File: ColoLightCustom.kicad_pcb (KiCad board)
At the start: 2 copper layers, 41.1 x 65.5 mm, 4 parts, among them J1 Conn_01x05_Male, J2 Conn_01x05_Male

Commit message: Version 0.1
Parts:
- added J3: Conn_01x03, halibs:SolderPads3, F.Cu at (142.2, 108.6)
- added J4: Conn_01x03_Male, Connector_PinHeader_2.54mm:PinHeader_1x03_P2.54mm_Vertical, F.Cu at (151.5, 73.4)
- added REF**: WEEE-Logo_4.2x6mm_SilkScreen, Symbol:WEEE-Logo_4.2x6mm_SilkScreen, B.Cu at (142.2, 103.5)
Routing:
- net Net-(J1-Pad3): track 0.00 -> 34.1 mm
- net +5V: track 16.1 -> 41.3 mm
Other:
- net class 5V added: clearance 0.3, trace_width 0.5, via_dia 0.8, via_drill 0.4
- board text added: "5V"
- board text added: "DIN"
- board text added: "GND"
- board text added: "haus-automatisierung.com v0.1"

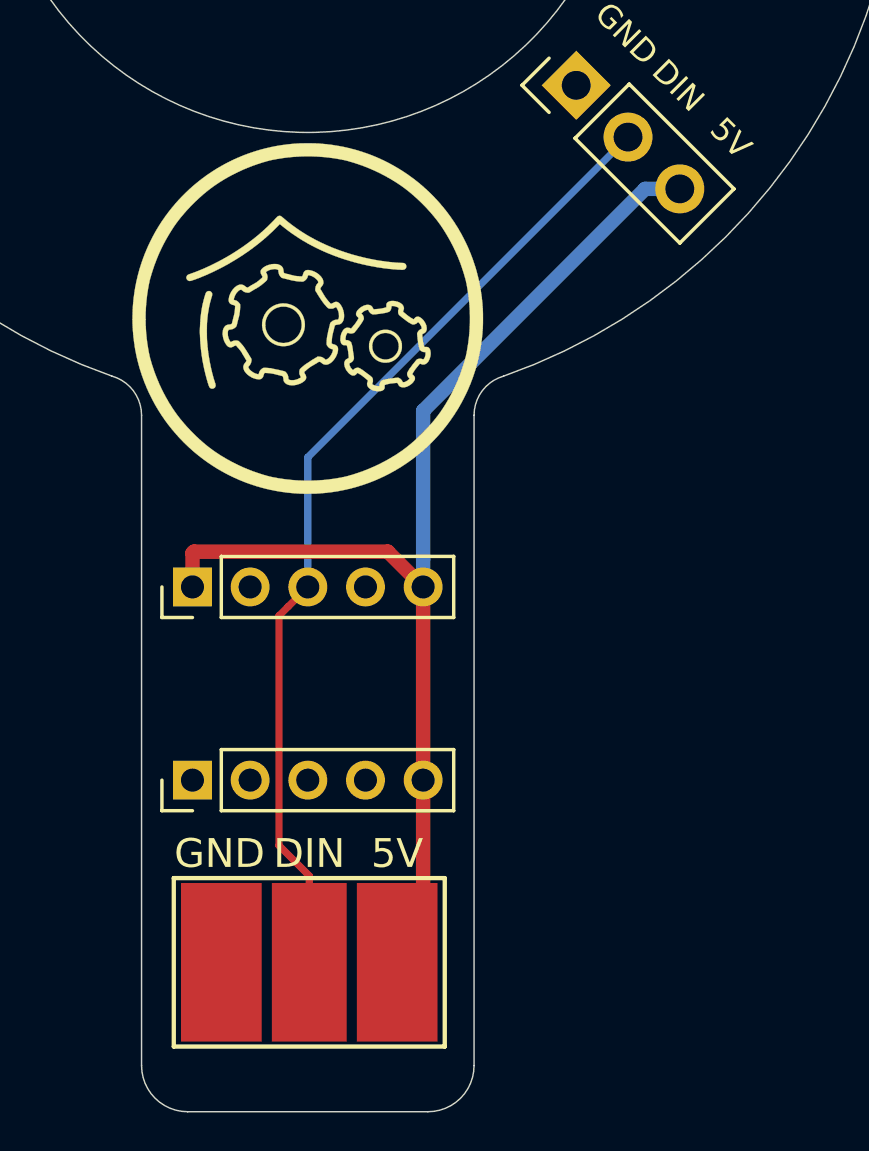
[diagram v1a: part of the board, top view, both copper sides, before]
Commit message: Changed thickness of lanes
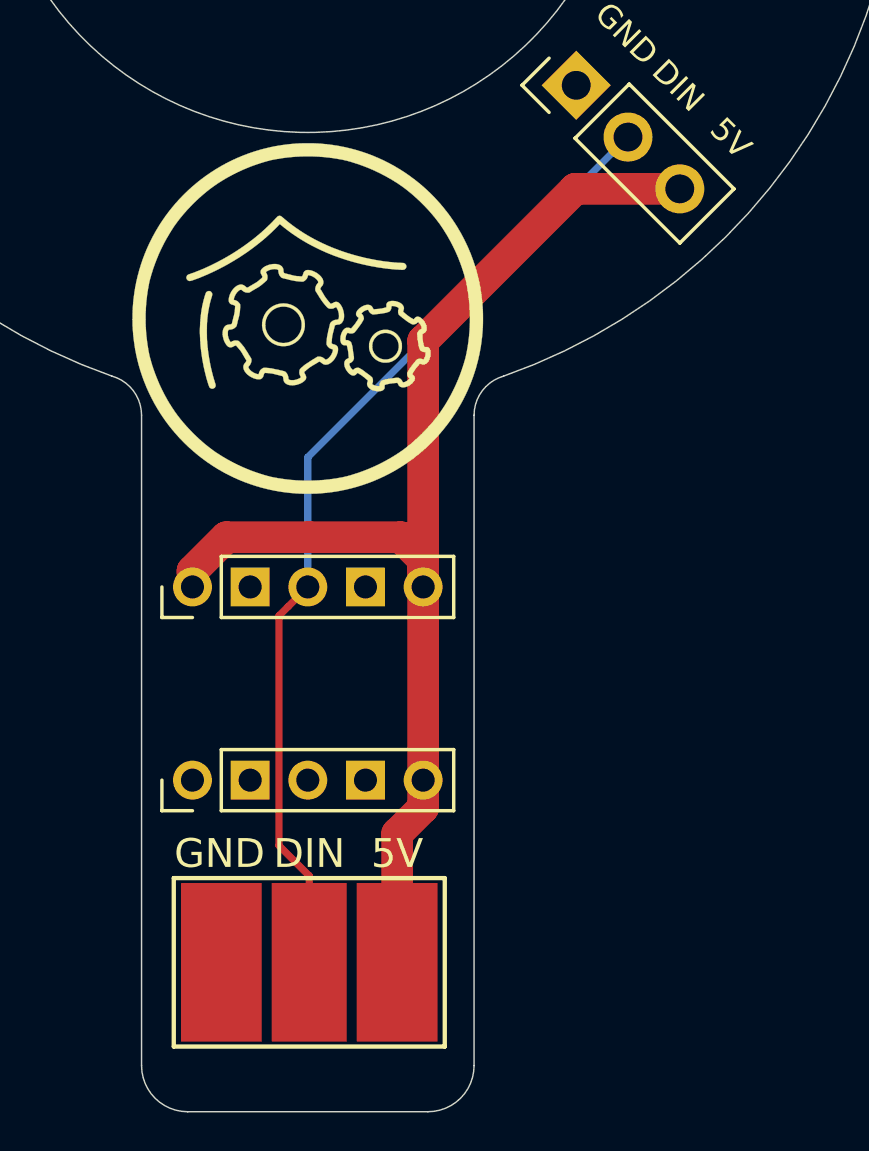
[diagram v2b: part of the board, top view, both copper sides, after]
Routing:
- net +5V: track 41.3 -> 43.3 mm
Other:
- net class 5V: clearance 0.3 -> 0.2; trace_width 0.5 -> 1.1
- board text added: "haus-automatisierung.com v0.2"
- board text removed: "haus-automatisierung.com v0.1"
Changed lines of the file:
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@@
     (thickness 1.6)
     (drawings 27)
-    (tracks 18)
+    (tracks 20)
     (zones 0)
     (modules 7)
@@
   (title_block
     (title "ColoLight Custom Controller")
-    (date 2019-11-17)
-    (rev 0.1)
+    (date 2019-11-19)
+    (rev 0.2)
     (company haus-automatisierung.com)
     (comment 1 "Matthias Kleine")
@@
     (mod_text_size 1 1)
     (mod_text_width 0.15)
-    (pad_size 2.6 5.5)
-    (pad_drill 0)
+    (pad_size 1.35 1.35)
+    (pad_drill 0.8)
     (pad_to_mask_clearance 0.051)
     (solder_mask_min_width 0.25)
@@
   )
   (net_class 5V ""
-    (clearance 0.3)
-    (trace_width 0.5)
+    (clearance 0.2)
+    (trace_width 1.1)
     (via_dia 0.8)
     (via_drill 0.4)
@@
     (pad 5 thru_hole oval (at 0 8 90) (size 1.35 1.35) (drill 0.8) (layers *.Cu *.Mask)
       (net 4 +5V))
-    (pad 4 thru_hole oval (at 0 6 90) (size 1.35 1.35) (drill 0.8) (layers *.Cu *.Mask)
+    (pad 4 thru_hole rect (at 0 6 90) (size 1.35 1.35) (drill 0.8) (layers *.Cu *.Mask)
       (net 5 GND))
     (pad 3 thru_hole oval (at 0 4 90) (size 1.35 1.35) (drill 0.8) (layers *.Cu *.Mask)
       (net 1 "Net-(J1-Pad3)"))
-    (pad 2 thru_hole oval (at 0 2 90) (size 1.35 1.35) (drill 0.8) (layers *.Cu *.Mask)
+    (pad 2 thru_hole rect (at 0 2 90) (size 1.35 1.35) (drill 0.8) (layers *.Cu *.Mask)
       (net 5 GND))
-    (pad 1 thru_hole rect (at 0 0 90) (size 1.35 1.35) (drill 0.8) (layers *.Cu *.Mask)
+    (pad 1 thru_hole circle (at 0 0 90) (size 1.35 1.35) (drill 0.8) (layers *.Cu *.Mask)
       (net 4 +5V))
     (model ${KISYS3DMOD}/Connector_PinHeader_2.00mm.3dshapes/PinHeader_1x05_P2.00mm_Vertical.wrl
@@
       (effects (font (size 1 1) (thickness 0.15)))
     )
-    (pad 1 thru_hole rect (at 0 0 90) (size 1.35 1.35) (drill 0.8) (layers *.Cu *.Mask)
+    (pad 1 thru_hole circle (at 0 0 90) (size 1.35 1.35) (drill 0.8) (layers *.Cu *.Mask)
       (net 2 "Net-(J2-Pad1)"))
-    (pad 2 thru_hole oval (at 0 2 90) (size 1.35 1.35) (drill 0.8) (layers *.Cu *.Mask)
+    (pad 2 thru_hole rect (at 0 2 90) (size 1.35 1.35) (drill 0.8) (layers *.Cu *.Mask)
       (net 5 GND))
     (pad 3 thru_hole oval (at 0 4 90) (size 1.35 1.35) (drill 0.8) (layers *.Cu *.Mask)
       (net 3 "Net-(J2-Pad3)"))
-    (pad 4 thru_hole oval (at 0 6 90) (size 1.35 1.35) (drill 0.8) (layers *.Cu *.Mask)
+    (pad 4 thru_hole rect (at 0 6 90) (size 1.35 1.35) (drill 0.8) (layers *.Cu *.Mask)
       (net 5 GND))
     (pad 5 thru_hole oval (at 0 8 90) (size 1.35 1.35) (drill 0.8) (layers *.Cu *.Mask)
@@
     )
   )
-  (gr_text "haus-automatisierung.com\nv0.1" (at 142.1638 49.5301) (layer B.SilkS)
+  (gr_text "haus-automatisierung.com\nv0.2" (at 142.1638 49.5301) (layer B.SilkS)
     (effects (font (size 1 1) (thickness 0.15)) (justify mirror))
   )
@@
   (segment (start 142.1638 86.345302) (end 142.1638 90.8422) (width 0.25) (layer B.Cu) (net 1))
   (segment (start 153.268951 75.240151) (end 142.1638 86.345302) (width 0.25) (layer B.Cu) (net 1))
-  (segment (start 146.1638 102.9594) (end 145.2626 103.8606) (width 0.5) (layer F.Cu) (net 4))
-  (segment (start 146.1638 97.5422) (end 146.1638 102.9594) (width 0.5) (layer F.Cu) (net 4))
-  (segment (start 146.1638 97.5422) (end 146.1638 90.8422) (width 0.5) (layer F.Cu) (net 4))
-  (segment (start 146.1638 89.887606) (end 146.1638 90.8422) (width 0.5) (layer B.Cu) (net 4))
-  (segment (start 146.1638 84.735323) (end 146.1638 89.887606) (width 0.5) (layer B.Cu) (net 4))
-  (segment (start 153.862921 77.036202) (end 146.1638 84.735323) (width 0.5) (layer B.Cu) (net 4))
-  (segment (start 155.065002 77.036202) (end 153.862921 77.036202) (width 0.5) (layer B.Cu) (net 4))
-  (segment (start 138.1638 89.6672) (end 138.1638 90.8422) (width 0.5) (layer F.Cu) (net 4))
-  (segment (start 144.938799 89.617199) (end 138.213801 89.617199) (width 0.5) (layer F.Cu) (net 4))
-  (segment (start 138.213801 89.617199) (end 138.1638 89.6672) (width 0.5) (layer F.Cu) (net 4))
-  (segment (start 146.1638 90.8422) (end 144.938799 89.617199) (width 0.5) (layer F.Cu) (net 4))
+  (segment (start 146.1638 98.496794) (end 145.2626 99.397994) (width 1.1) (layer F.Cu) (net 4))
+  (segment (start 145.2626 99.397994) (end 145.2626 103.8606) (width 1.1) (layer F.Cu) (net 4))
+  (segment (start 146.1638 97.5422) (end 146.1638 98.496794) (width 1.1) (layer F.Cu) (net 4))
+  (segment (start 146.1638 97.5422) (end 146.1638 90.8422) (width 1.1) (layer F.Cu) (net 4))
+  (segment (start 139.335799 89.117199) (end 138.1638 90.289198) (width 1.1) (layer F.Cu) (net 4))
+  (segment (start 146.1638 89.887606) (end 145.393393 89.117199) (width 1.1) (layer F.Cu) (net 4))
+  (segment (start 138.1638 90.289198) (end 138.1638 90.8422) (width 1.1) (layer F.Cu) (net 4))
+  (segment (start 146.1638 90.8422) (end 146.1638 89.887606) (width 1.1) (layer F.Cu) (net 4))
+  (segment (start 142.213301 89.117199) (end 139.335799 89.117199) (width 1.1) (layer F.Cu) (net 4))
+  (segment (start 145.393393 89.117199) (end 142.213301 89.117199) (width 1.1) (layer F.Cu) (net 4))
+  (segment (start 155.065002 77.036202) (end 151.436798 77.036202) (width 1.1) (layer F.Cu) (net 4))
+  (segment (start 146.1638 82.3092) (end 146.1638 90.8422) (width 1.1) (layer F.Cu) (net 4))
+  (segment (start 151.436798 77.036202) (end 146.1638 82.3092) (width 1.1) (layer F.Cu) (net 4))
   (zone (net 5) (net_name GND) (layer B.Cu) (hatch edge 0.508)
     (connect_pads (clearance 0.508))

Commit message: Removed old logo
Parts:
- removed G*** (x2): LOGO, halibs:Logo
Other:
- net class 5V removed
- net class Default removed
- board text added: "haus-automatisierung.com v0.3"
- board text removed: "haus-automatisierung.com v0.2"

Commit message: Updated PCB preview
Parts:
- added G***: LOGO, haus-automatisierung:Logo2024-notext, F.Cu at (142.2, 80.5)
- moved REF** 0.50 mm to (142.2, 104.0)
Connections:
- J2 pad 1: Net-(J2-Pad1) -> unconnected-(J2-Pin_1-Pad1)
- J2 pad 3: Net-(J2-Pad3) -> unconnected-(J2-Pin_3-Pad3)

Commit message: v0.3
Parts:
- J3: footprint halibs:SolderPads3 -> haus-automatisierung:SolderPads3
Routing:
- net +5V: track 43.3 -> 43.8 mm
- net Net-(J1-Pin_3): vias 0 -> 1
